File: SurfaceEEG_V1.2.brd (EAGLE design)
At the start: 160 x 100 mm, 70 parts, among them IC1 LMV602, IC2 TSZ124IQ4T, U1 MCP4442-103E/ST

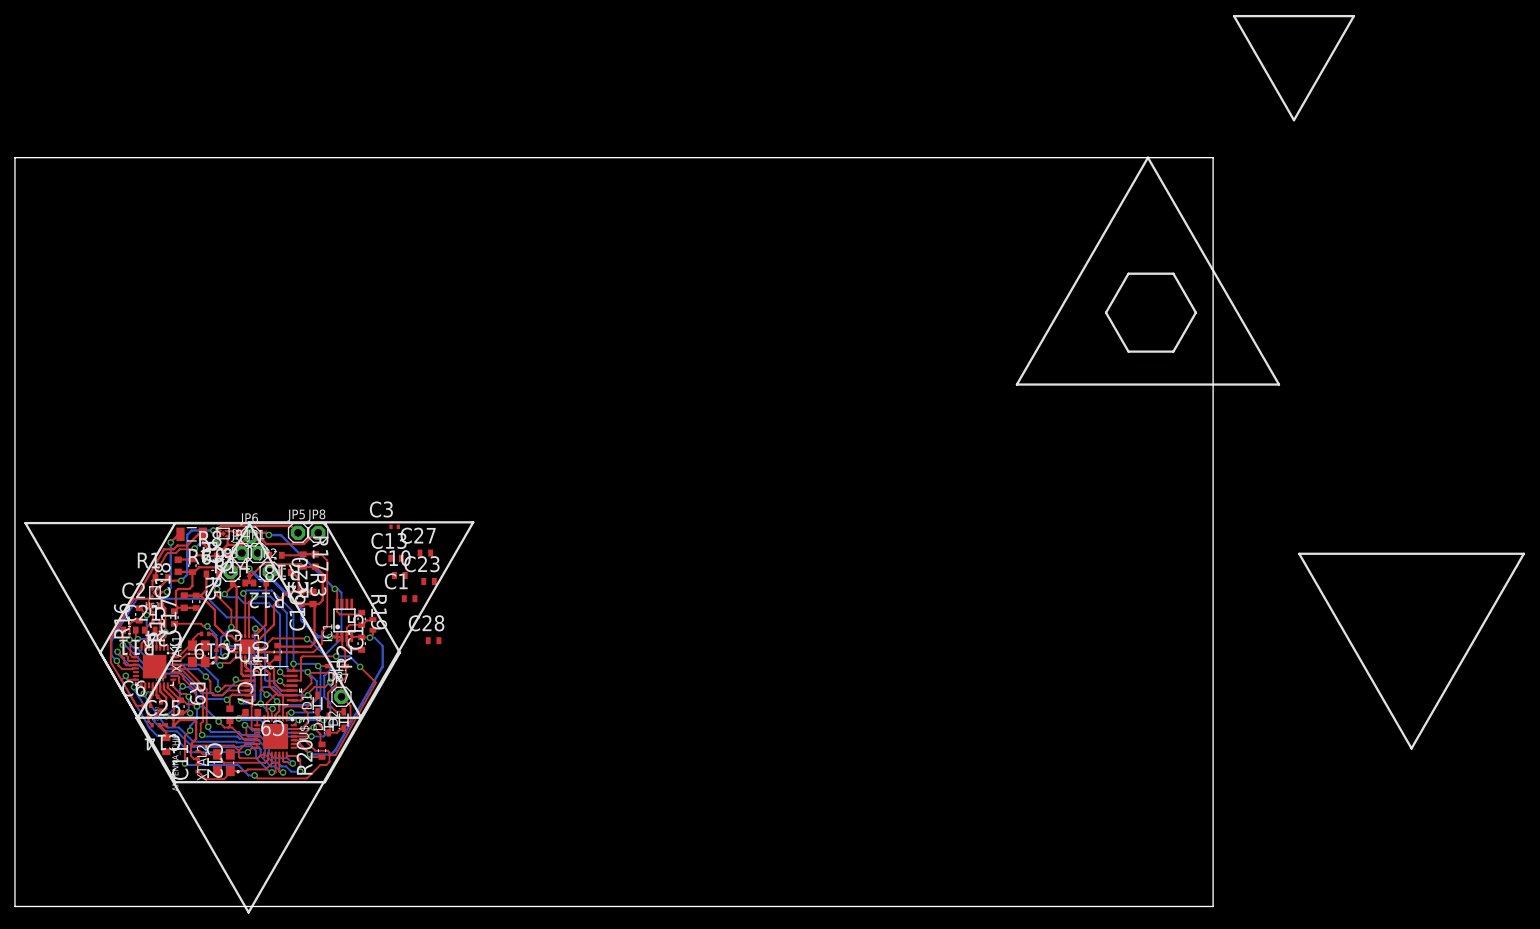
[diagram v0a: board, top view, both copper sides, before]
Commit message: Finished PCB and updated schematics
Added headers for sensor board connection and placed/routed remaining caps, optimized everything
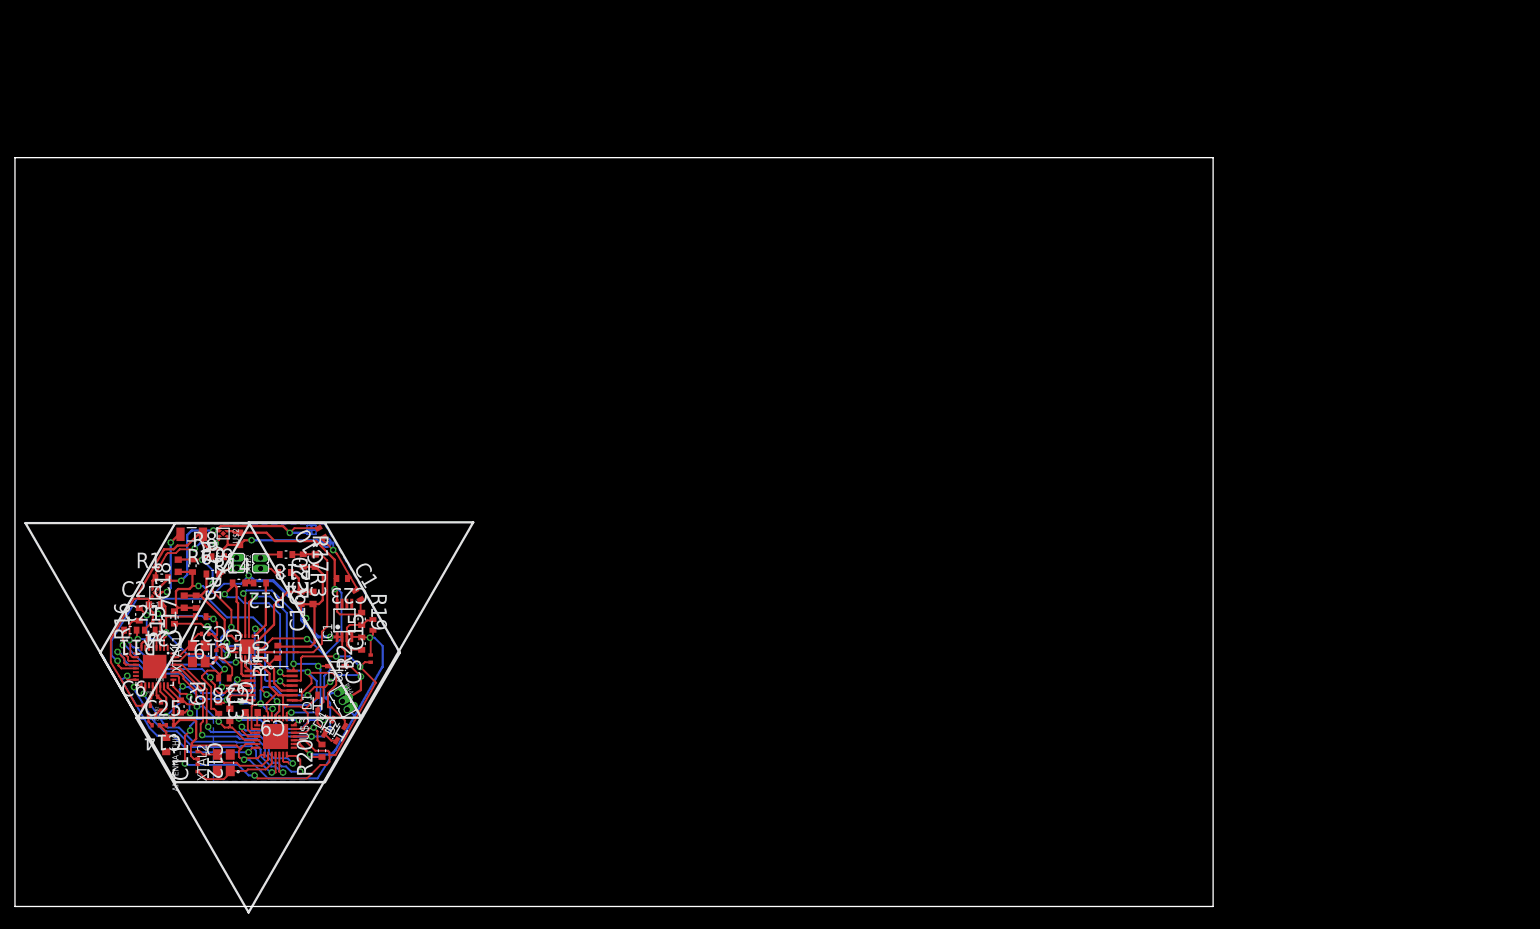
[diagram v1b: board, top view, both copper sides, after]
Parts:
- removed JP1, JP2, JP3, JP4, JP5, JP6, JP7, JP8: (no value), adafruit:1X01
- added PH1, PH2: PH1X2-05LONGSNAP, pel_hdr:PHLS005-1-2
- added PH4: PH1X3, (misc)-parts-that-we-use:PH005-1-3
- added U$4: VCC, (custom)-new-components:VCC-PAD
- added U$5: GND, (custom)-new-components:GND-PAD
- moved C27 31.2 mm to (24.8, 38.7), turned to 180 degrees
- moved C13 31.0 mm to (27.2, 26.5), turned to 270 degrees
- moved C28 28.4 mm to (27.9, 30.5), turned to 180 degrees
- moved C3 17.9 mm to (47.5, 33.1), turned to 90 degrees
- moved C10 11.9 mm to (40.9, 49.9), turned to 120 degrees
- moved C23 11.6 mm to (43.7, 43.8), turned to 180 degrees
- moved C1 6.92 mm to (45.8, 41.6), turned to 300 degrees
- moved D2 1.84 mm to (43.5, 23.1), turned to 60 degrees
- moved R18 1.40 mm to (36.2, 47.0)
- moved R8 0.71 mm to (27.1, 46.7)
- moved D4 0.30 mm to (41.9, 24.0), turned to 60 degrees
- moved C2 0.20 mm to (18.7, 40.3)
- moved R11 0.10 mm to (15.4, 36.9)
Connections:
- net CH0: now also PH1.2; no longer JP1.1
- net CH1: now also PH1.1; no longer JP2.1
- net CH2: now also PH2.2; no longer JP3.1
- net CH3: now also PH2.1; no longer JP4.1
- net GND: now also PH4.P$3, U$5.P$1; no longer JP6.1, JP8.1
- net GNDI: now also PH4.P$2; no longer JP7.1
- net VDD: now also PH4.P$1
- net VIN: now also U$4.P$1; no longer JP5.1
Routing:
- net GND: track 159.2 -> 209.0 mm, vias 6 -> 11
- net VCC: track 116.3 -> 144.1 mm, vias 12 -> 13
- net VDD: track 73.7 -> 80.2 mm, vias 5 -> 4
- net VIN: track 26.5 -> 32.5 mm, vias 2 -> 3
- net AGND: track 18.9 -> 22.8 mm
- net CH2: track 0.00 -> 2.67 mm
- net CH1: track 0.00 -> 2.58 mm
- net CH3_F: track 23.7 -> 21.3 mm
- net GNDI: track 112.1 -> 110.0 mm, vias 6 -> 9
- net CH3: track 0.00 -> 1.71 mm
- net CH1_F_A: track 51.3 -> 52.7 mm
- net P3B: track 17.4 -> 16.2 mm
- net CH0_F: track 26.9 -> 25.7 mm
- net CH0: track 1.69 -> 2.75 mm
- net CH3_F_A: track 22.5 -> 23.2 mm
- added copper zone on layer 16, net GND
